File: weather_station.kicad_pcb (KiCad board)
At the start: 2 copper layers, 24 x 57.8 mm, 75 parts, among them J1 Conn_01x03, J2 Conn_01x05_Male, J3 Conn_01x05, J4 Conn_02x04_Odd_Even, J5 USB_B_Micro, P1 USB_C_Plug, Q1 BSS138, Q2 BSS84, Q3 BSS84, Q4 BSS138_NC, Q5 BSS138, SW1 SW_Push, U1 ESP-12F, U2 AMS1117-3.3, U3 LM75B, U4 BME280, U5 BME680

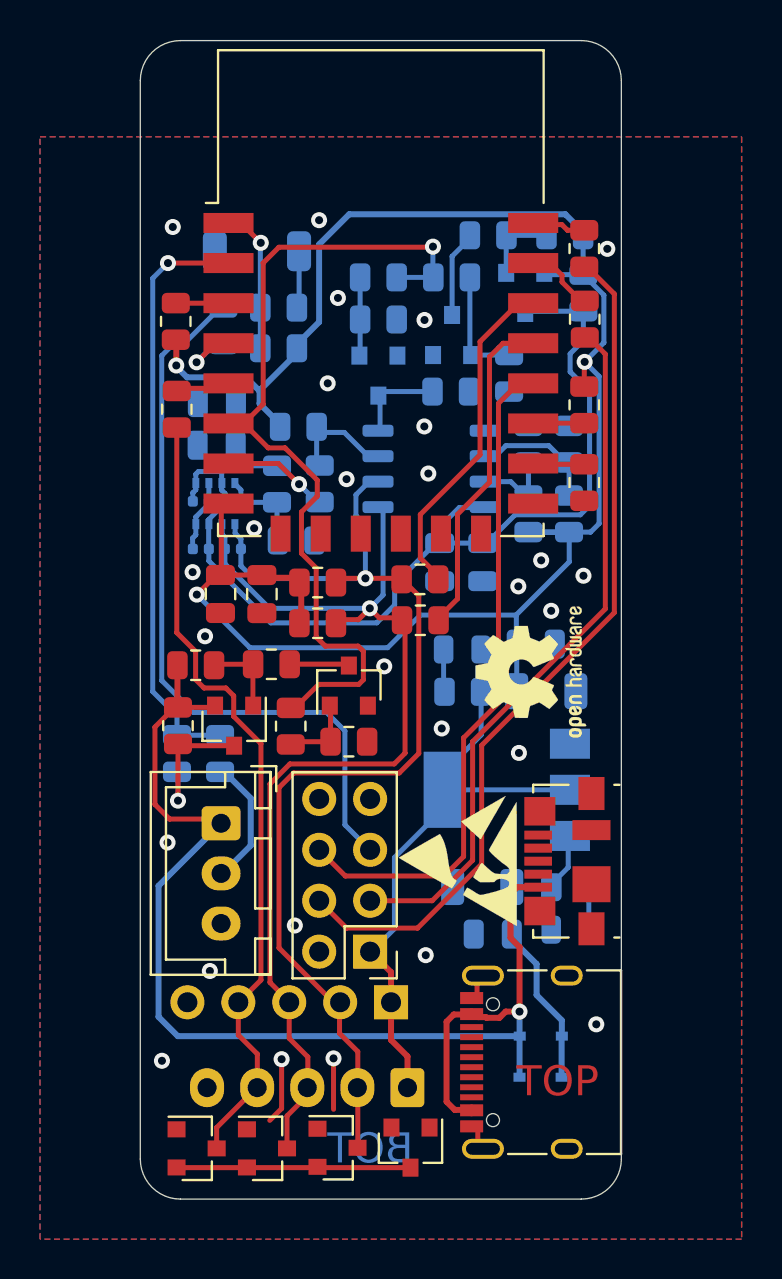
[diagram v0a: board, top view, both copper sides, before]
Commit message: Edit NC Components and update footprints
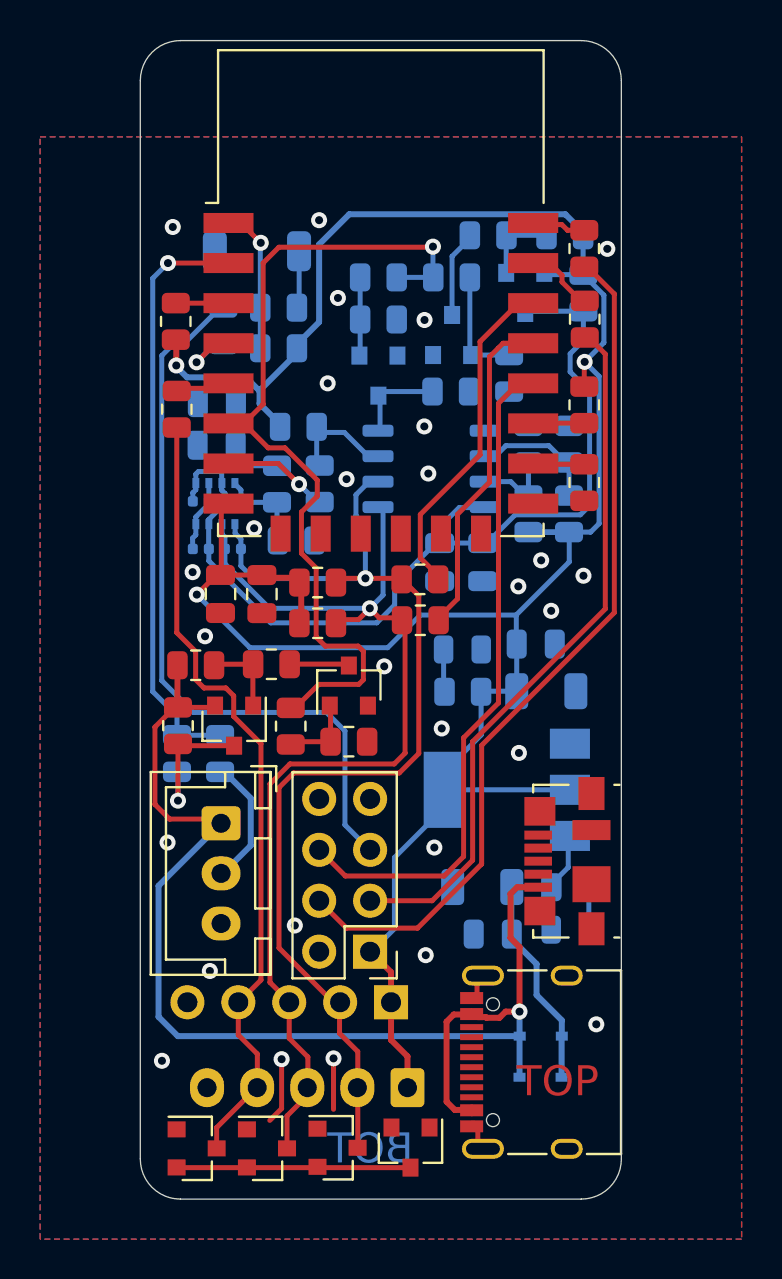
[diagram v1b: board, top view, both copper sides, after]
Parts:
- removed REF**: ESD-Logo_6.6x6mm_SilkScreen, Symbol:ESD-Logo_6.6x6mm_SilkScreen
- removed REF**: OSHW-Logo2_7.3x6mm_SilkScreen, Symbol:OSHW-Logo2_7.3x6mm_SilkScreen
- D3: value BAT48JFILM -> NC_BAT48JFILM
- D7: value LED_GREEN -> NC_LED_GREEN
- D8: value LED_RED -> NC_LED_RED
- Q4: value BSS138_NC -> NC_BSS138
- R10, R25: value 0R_NC -> NC_0R
- R18: value 0R_NC -> 0R
- R20, R21: value 470R -> NC_470R
- R28: value 10kR_NC -> NC_10kR
- R30: value 100R_NC -> NC_100R
- R31, R33: value 0R_NC -> NC_100R
- R32, R34, R38: value 0R -> 100R
- R37: value 0R -> NC_100R
- U5: value BME680 -> NC_BME680
